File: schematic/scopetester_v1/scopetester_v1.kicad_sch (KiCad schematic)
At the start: 43 parts, among them J1 CON_PWR, J2 Conn_01x04, J3 AVR_ISP, SW1 SW_Push, U1 ATmega8A-P, Y1 16MHz

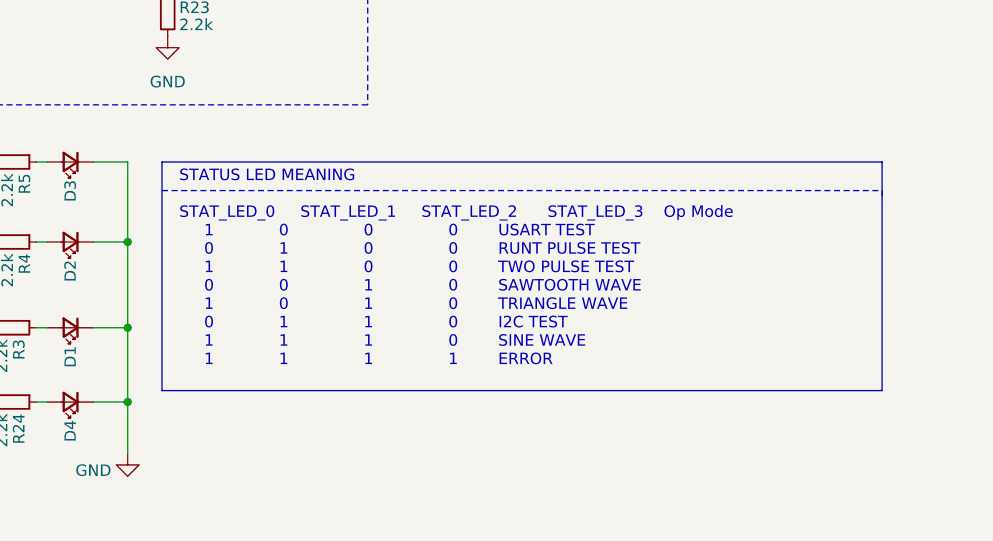
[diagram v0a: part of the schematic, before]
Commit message: Minor changes to comments in schematic
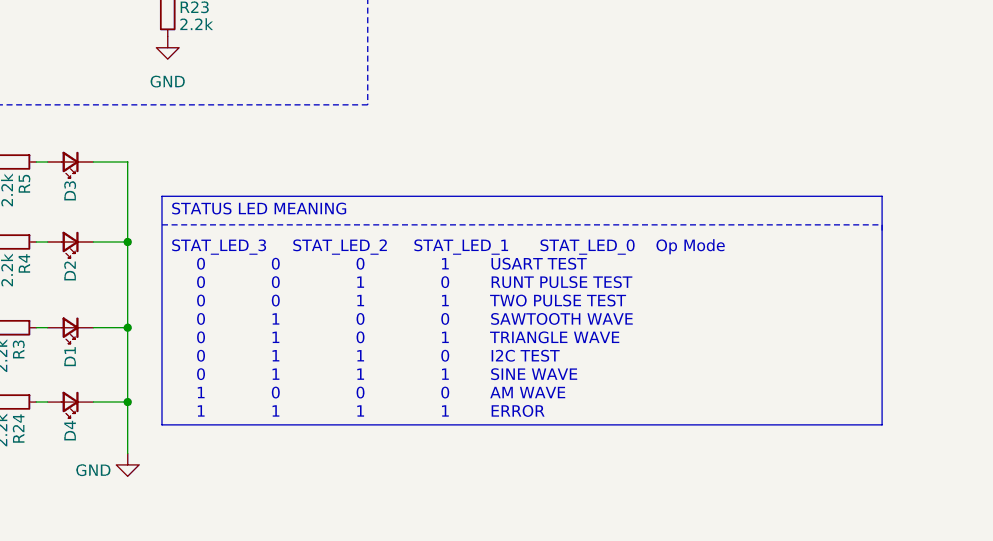
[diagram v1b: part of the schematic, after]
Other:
- note added: "STATUS LED MEANING STAT_LED_3 STAT_LED_2 STAT_LED_1 STAT_LED_0 Op Mode 0 0 0 1 USART TEST 0 0 1 0 RUNT PULSE TEST 0 0 1 1 TWO PULSE TEST 0 1 0 0 SAWTOOTH WAVE 0 1 0 1 TRIANGLE WAVE 0 1 1 0 I2C TEST 0 1 1 1 SINE WAVE 1 0 0 0 AM WAVE 1 1 1 1 ERROR"
- note removed: "STATUS LED MEANING STAT_LED_0 STAT_LED_1 STAT_LED_2 STAT_LED_3 Op Mode 1 0 0 0 USART TEST 0 1 0 0 RUNT PULSE TEST 1 1 0 0 TWO PULSE TEST 0 0 1 0 SAWTOOTH WAVE 1 0 1 0 TRIANGLE WAVE 0 1 1 0 I2C TEST 1 1 1 0 SINE WAVE 1 1 1 1 ERROR"
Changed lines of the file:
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@@
 		)
 	)
-	(text "STATUS LED MEANING\n\nSTAT_LED_0     STAT_LED_1     STAT_LED_2      STAT_LED_3    Op Mode\n     1             0               0               0        USART TEST\n     0             1               0               0        RUNT PULSE TEST\n     1             1               0               0        TWO PULSE TEST\n     0             0               1               0        SAWTOOTH WAVE\n     1             0               1               0        TRIANGLE WAVE\n     0             1               1               0        I2C TEST\n     1             1               1               0        SINE WAVE\n     1             1               1               1        ERROR"
+	(text "STATUS LED MEANING\n\nSTAT_LED_3     STAT_LED_2     STAT_LED_1      STAT_LED_0    Op Mode\n     0             0               0               1        USART TEST\n     0             0               1               0        RUNT PULSE TEST\n     0             0               1               1        TWO PULSE TEST\n     0             1               0               0        SAWTOOTH WAVE\n     0             1               0               1        TRIANGLE WAVE\n     0             1               1               0        I2C TEST\n     0             1               1               1        SINE WAVE\n     1             0               0               0        AM WAVE\n     1             1               1               1        ERROR"
 		(exclude_from_sim no)
-		(at 202.565 144.78 0)
+		(at 201.676 150.622 0)
 		(effects
 			(font
@@
 	(polyline
 		(pts
-			(xy 280.67 121.92) (xy 200.66 121.92)
+			(xy 280.67 125.73) (xy 200.66 125.73)
 		)
 		(stroke
@@
 	(polyline
 		(pts
-			(xy 200.66 121.92) (xy 200.66 147.32)
+			(xy 200.66 125.73) (xy 200.66 151.13)
 		)
 		(stroke
@@
 	(polyline
 		(pts
-			(xy 280.67 125.73) (xy 280.67 125.095)
+			(xy 280.67 129.54) (xy 280.67 128.905)
 		)
 		(stroke
@@
 	(polyline
 		(pts
-			(xy 280.67 147.32) (xy 280.67 121.92)
+			(xy 280.67 151.13) (xy 280.67 125.73)
 		)
 		(stroke
@@
 	(polyline
 		(pts
-			(xy 200.66 125.095) (xy 280.67 125.095)
+			(xy 200.66 128.905) (xy 280.67 128.905)
 		)
 		(stroke
@@
 	(polyline
 		(pts
-			(xy 200.66 147.32) (xy 280.67 147.32)
-		)
-		(stroke
+			(xy 200.66 151.13) (xy 280.67 151.13)
+		)
+		(stroke

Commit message: Minor updates to PCB layout
Also includes:
* Cap C5 changes to 10uF from 1uF
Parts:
- C5: value 1uF -> 10uF
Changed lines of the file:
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@@
 			)
 		)
-		(property "Value" "1uF"
+		(property "Value" "10uF"
 			(at 111.76 51.1809 0)
 			(effects

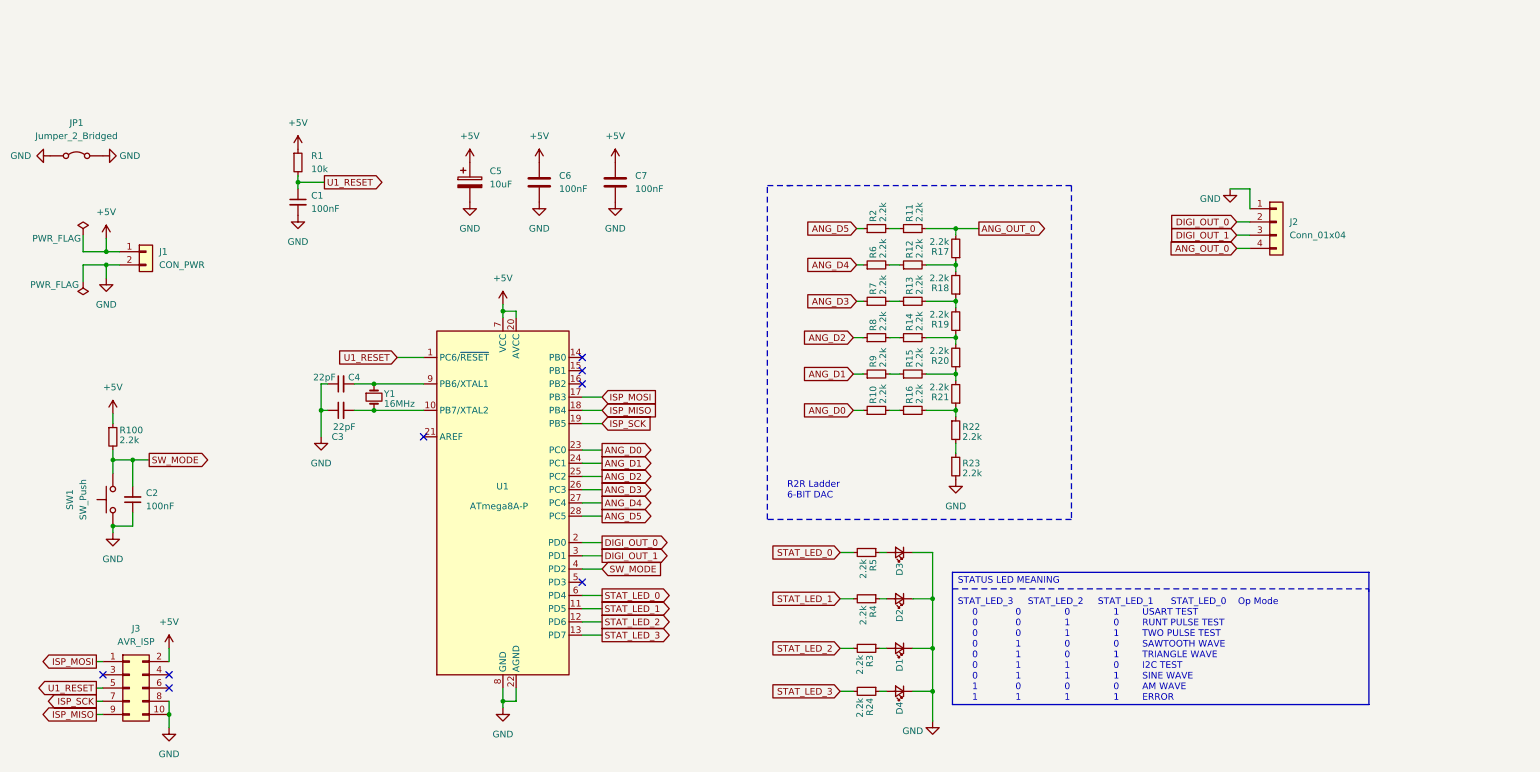
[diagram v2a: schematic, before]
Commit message: hw: Added info about outputs depending on modes
Also includes:
* Title update in the schematic. ScopeTester -> signal.echo.
* GitHub repo link added to schematic description.
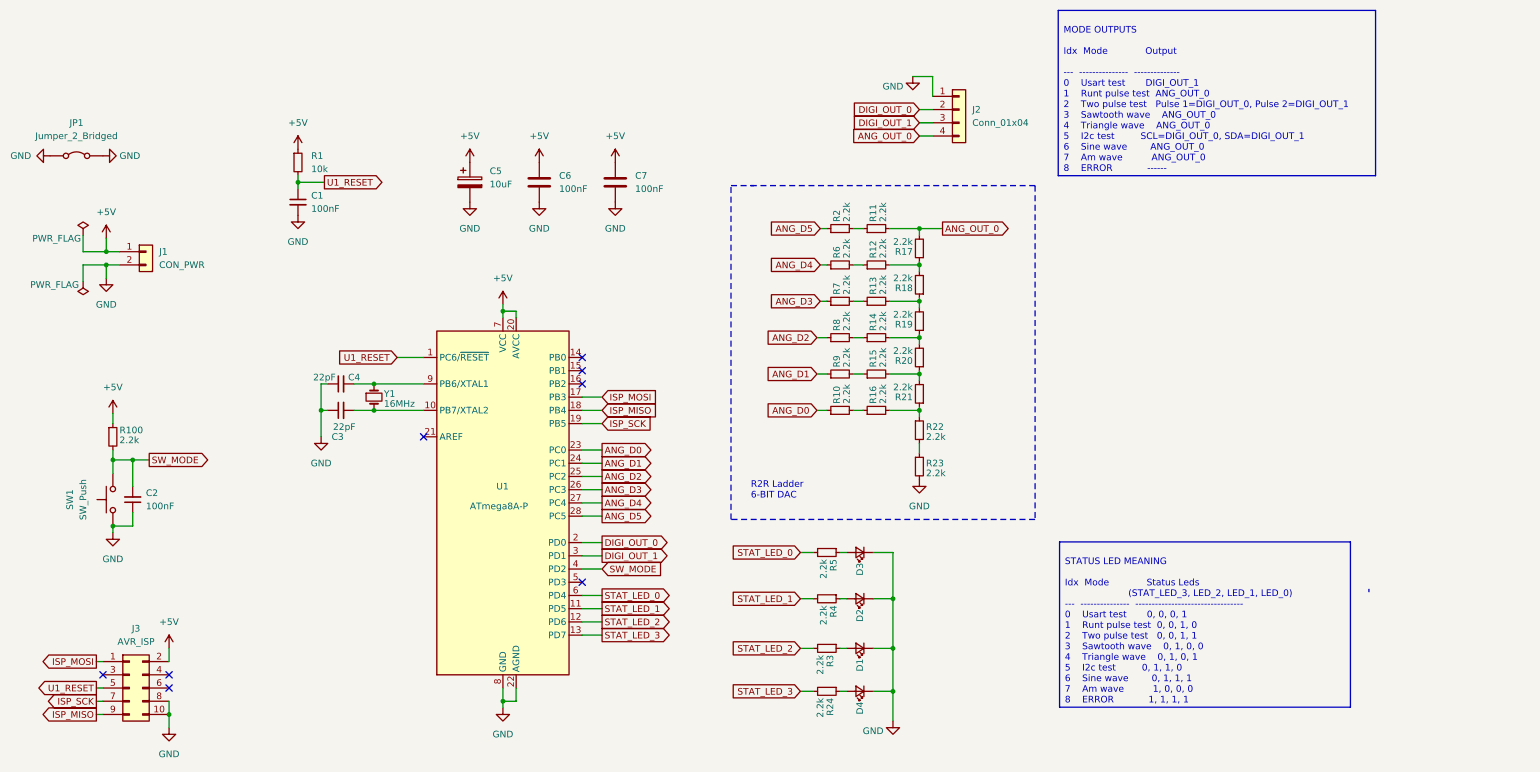
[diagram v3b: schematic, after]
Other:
- note added: "MODE OUTPUTS Idx Mode Output --- --------------- -------------- 0 Usart test DIGI_OUT_1 1 Runt pulse test ANG_OUT_0 2 Two pulse test Pulse 1=DIGI_OUT_0, Pulse 2=DIGI_OUT_1 3 Sawtooth wave ANG_OUT_0 4 Triangle wave ANG_OUT_0 5 I2c test SCL=DIGI_OUT_0, SDA=DIGI_OUT_1 6 Sine wave ANG_OUT_0 7 Am wave ANG_OUT_0 8 ERROR ------"
- note added: "STATUS LED MEANING Idx Mode Status Leds (STAT_LED_3, LED_2, LED_1, LED_0) --- --------------- --------------------------------- 0 Usart test 0, 0, 0, 1 1 Runt pulse test 0, 0, 1, 0 2 Two pulse test 0, 0, 1, 1 3 Sawtooth wave 0, 1, 0, 0 4 Triangle wave 0, 1, 0, 1 5 I2c test 0, 1, 1, 0 6 Sine wave 0, 1, 1, 1 7 Am wave 1, 0, 0, 0 8 ERROR 1, 1, 1, 1"
- note removed: "STATUS LED MEANING STAT_LED_3 STAT_LED_2 STAT_LED_1 STAT_LED_0 Op Mode 0 0 0 1 USART TEST 0 0 1 0 RUNT PULSE TEST 0 0 1 1 TWO PULSE TEST 0 1 0 0 SAWTOOTH WAVE 0 1 0 1 TRIANGLE WAVE 0 1 1 0 I2C TEST 0 1 1 1 SINE WAVE 1 0 0 0 AM WAVE 1 1 1 1 ERROR"
- company: (none) -> https://github.com/coderarjob/signal.echo
- title: ScopeTester -> signal.echo
- moved on the sheet: D1, D2, D3, D4, J2, R10, R11, R12, R13, R14, R15, R16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
